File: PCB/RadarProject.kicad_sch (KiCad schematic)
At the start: 68 parts, among them J1 Conn_Coaxial, J2 Conn_Coaxial, J3 Conn_01x05, Q1 2N7000, SW1 SW_SPDT, U1 AT0603T03ECATD, U2 PD2328J5050S2HF, U3 BGU8052, U4 BGU8052, U5 RQRA-2328-2536-CR, U6 HMC213B, U7 LMC6484, U8 LMC6484

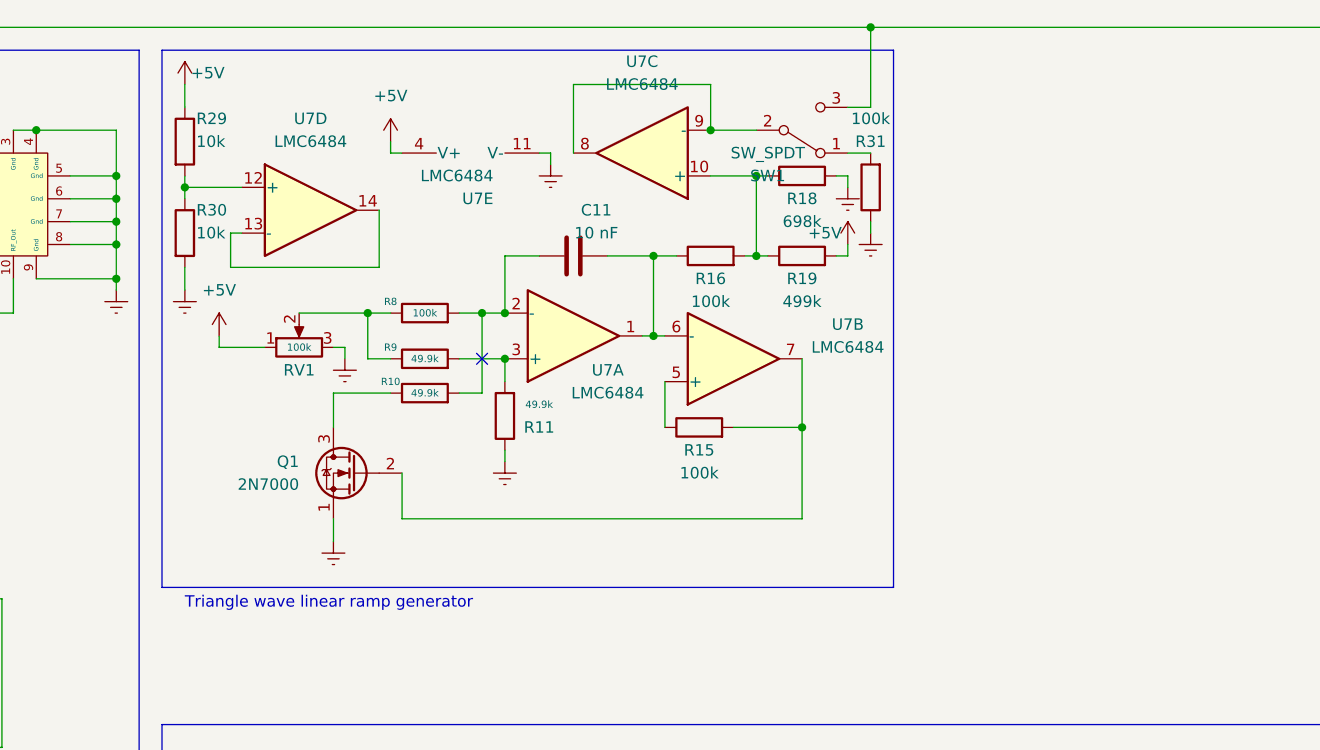
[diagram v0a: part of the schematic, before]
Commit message: Final schematic is generally done, just some minor fixes
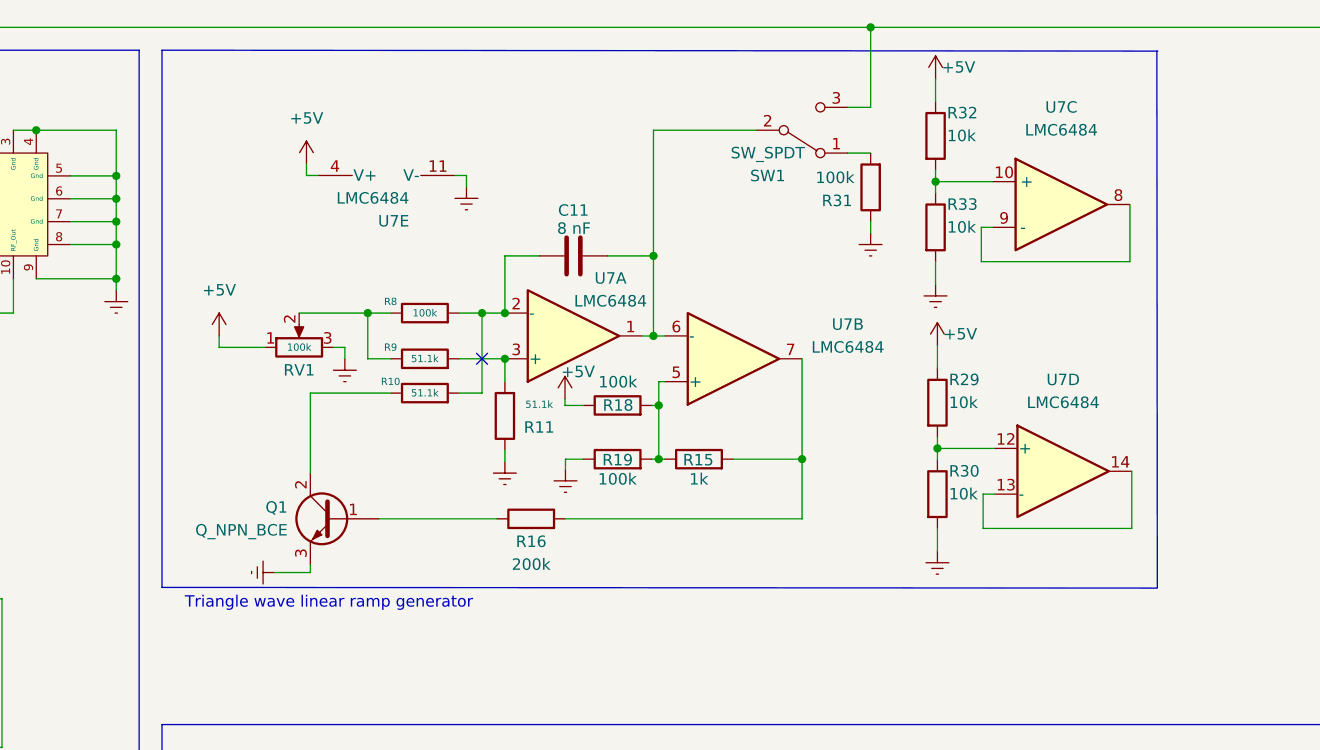
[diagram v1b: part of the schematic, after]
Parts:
- removed Q1: 2N7000, Package_TO_SOT_THT:TO-92_Inline, symbol Transistor_FET:2N7000
- removed unit 3 of U7
- added Q1: Q_NPN_BCE, Package_TO_SOT_THT:TO-92L_Inline, symbol Device:Q_NPN_BCE
- added R32, R33: 10k, Resistor_SMD:R_0805_2012Metric, symbol Device:R
- added unit 3 of U7
- C11: value 10 nF -> 8 nF
- R10, R11, R9: value 49.9k -> 51.1k
- R15: value 100k -> 1k
- R16: value 100k -> 200k
- R18: value 698k -> 100k
- R19: value 499k -> 100k
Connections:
- net +5V: now also R18.1, R32.1; no longer R19.2
- net Earth: now also R19.1, Q1.3 (E), R33.2; no longer R18.2
- net at SW1.2 (B): now also C11.2, U7.1, U7.6 (-)
- net at R10.1: now also Q1.2 (C)
- net at R15.2, U7.7: now also R16.2
- net at R15.1, U7.5 (+): now also R18.2, R19.2
- new net: Q1.1 (B), R16.1
- new net: R32.2, R33.1, U7.10 (+)
- new net: U7.8, U7.9 (-)
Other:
- moved on the sheet: R15, R29, R30, U7D, U7E

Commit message: Updated PCB, added antennas, etc.
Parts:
- removed AE1, AE2: Antenna, symbol Device:Antenna
- added AE1, AE2: Antenna_Loop, symbol Device:Antenna_Loop
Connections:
- net Earth: now also R31.2, AE1.1, AE2.1; no longer R31.1
- net at SW1.1 (A): now also C11.2, U7.1, U7.6 (-); no longer R31.2
- net at J3.5 (Pin_5), U5.2 (Vt): now also SW1.2 (B); no longer SW1.3 (C)
- net at J2.2 (Ext): now also AE2.2
- net at J1.2 (Ext): now also AE1.2
- new net: R31.1, SW1.3 (C)
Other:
- moved on the sheet: R31, SW1

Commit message: new version of PCB
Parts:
- removed R29, R30: 10k, Resistor_SMD:R_0805_2012Metric, symbol Device:R
- removed U5: RQRA-2328-2536-CR, RadarProject:RQRA-2328-2536-CR, symbol RadarProject:RQRA-2328-2536-CR
- added U5: CVCO55CC-2230-2430, RadarProject:CVCO55CC-2230-2430, symbol RadarProject:CVCO55CC-2230-2430
- J1, J2: footprint Connector_Coaxial:SMA_Amphenol_132289_EdgeMount -> Connector_Coaxial:SMA_Samtec_SMA-J-P-X-ST-EM1_EdgeMount
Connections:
- net +5V: now also U5.14 (Vcc)
- net Earth: now also Q1.1 (E), U5.1 (Gnd), U5.11 (Gnd), U5.12 (Gnd), U5.13 (Gnd), U5.15 (Gnd), U5.16 (Gnd), U5.3 (Gnd), U5.4 (Gnd), U5.5 (Gnd), U5.6 (Gnd), U5.7 (Gnd), U5.8, U5.9 (Gnd); no longer Q1.3 (E)
- net at U7.12 (+): now also C11.2, U7.1, U7.6 (-)
- net at J3.5 (Pin_5), SW1.2 (B): now also U5.2 (Vt)
- net at R16.1: now also Q1.2 (C); no longer Q1.1 (B)
- net at R10.1: now also Q1.3 (B); no longer Q1.2 (C)
- net at U1.1 (RF_in): now also U5.10 (RF_Out)
- net at U7.13 (-), U7.14: now also SW1.1 (A)
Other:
- moved on the sheet: Q1, U7D, U7E
